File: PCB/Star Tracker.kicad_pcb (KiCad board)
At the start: 2 copper layers, 76.2 x 42.5 mm, 33 parts, among them J1 Conn_ARM_JTAG_SWD_10, U1 NCV565D2TG-ND, U2 DRV8833PW, U3 ATSAMD21E18A-AU, U4 AP7312-1833W6-7

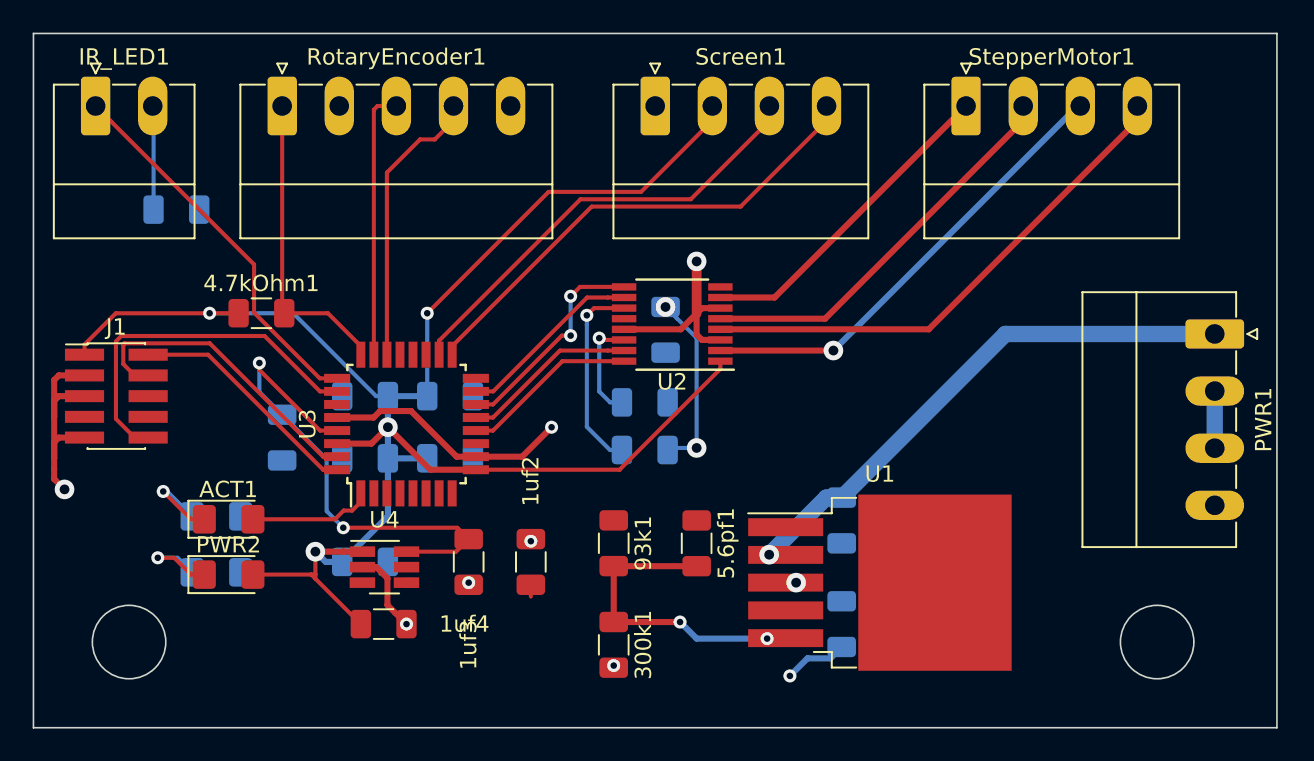
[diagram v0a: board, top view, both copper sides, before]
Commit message: Finished layout and greated gerbers. Off to fab!
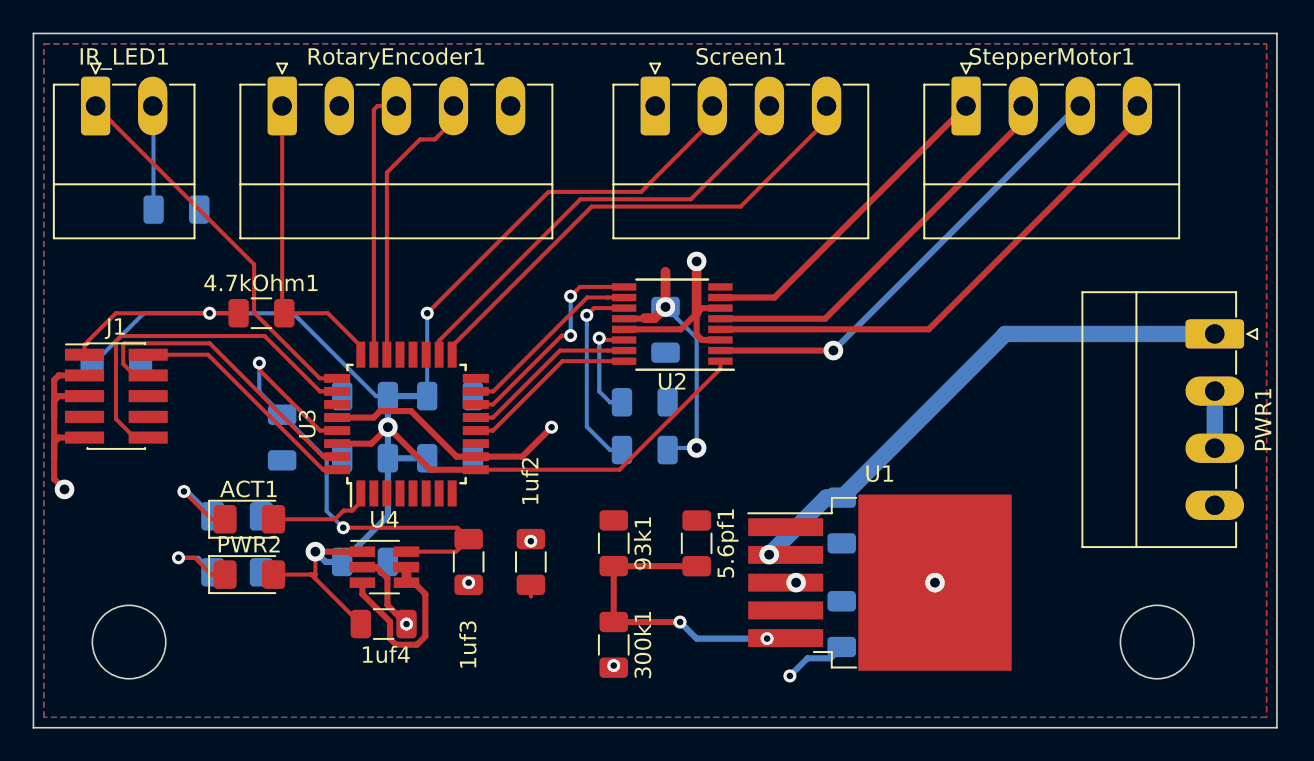
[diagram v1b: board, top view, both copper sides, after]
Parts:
- added 1uf5: C, Capacitor_SMD:C_1206_3216Metric_Pad1.42x1.75mm_HandSolder, B.Cu at (109.2, 73.0)
- moved ACT1 1.27 mm to (117.4, 82.5)
- moved PWR2 1.27 mm to (117.4, 85.9)
- moved 330Ohm2 1.27 mm to (116.6, 85.7)
- moved 330Ohm3 1.27 mm to (116.6, 82.3)
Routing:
- net 3V8: track 16.5 -> 34.3 mm
- net 3V3: track 111.0 -> 118.2 mm
- net ACT: track 7.58 -> 6.31 mm
- net GND: vias 8 -> 9
- added copper zone on F.Cu, net 3V8
- added copper zone on B.Cu, net GND
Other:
- board text added: "Star Tracking Camera Mount Control Board Design By: Michael Greer"

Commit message: Swapped 93k and 300k resistors
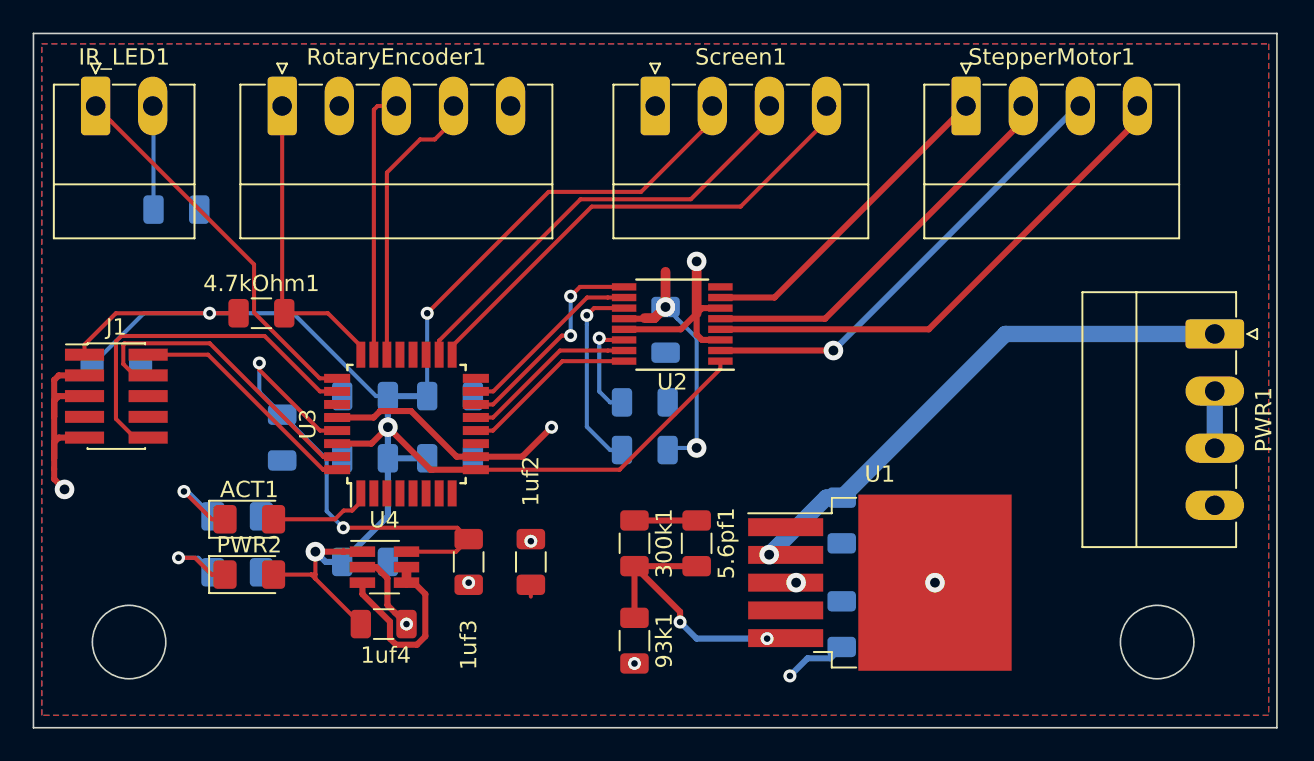
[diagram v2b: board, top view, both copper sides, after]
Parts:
- moved 300k1 6.35 mm to (141.0, 83.9)
- moved 93k1 6.10 mm to (141.0, 89.9)
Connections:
- 300k1 pad 1: Net-(300k1-Pad1) -> 3V8
- 300k1 pad 2: GND -> Net-(300k1-Pad2)
- 5.6pf1 pad 2: Net-(300k1-Pad1) -> Net-(300k1-Pad2)
- 93k1 pad 1: 3V8 -> Net-(300k1-Pad2)
- 93k1 pad 2: Net-(300k1-Pad1) -> GND
- U1 pad 5: Net-(300k1-Pad1) -> Net-(300k1-Pad2)
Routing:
- net Net-(300k1-Pad1): track 18.3 -> 0.00 mm, vias 2 -> 0
- net Net-(300k1-Pad2): track 0.00 -> 17.3 mm, vias 0 -> 2
- net 3V8: track 34.3 -> 38.1 mm
